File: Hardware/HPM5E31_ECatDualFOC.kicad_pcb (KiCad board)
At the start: 4 copper layers, 85 x 113.4 mm, 453 parts, among them J1 Conn_Coaxial, J13 PHB2.0-02-20PWZ, J14 PHB2.0-02-20PWZ, J15 RJ45_Hanrun_HR911105A_Horizon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, J16 RJ45_Hanrun_HR911105A_Horizon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, J17 WAFER-GH1.25-4PWB, J18 WAFER-GH1.25-4PWB, J19 WAFER-GH1.25-4PWB, J2 Conn_Coaxial, J20 WAFER-GH1.25-2PWB, J21 WAFER-GH1.25-2PWB, J22 USB_B, J23 WAFER-GH1.25-4PWB, J24 WAFER-GH1.25-4PLB, J3 WAFER-ZH1.5-4PWB, J4 Conn_02x05_Odd_Even, J5 WAFER-GH1.25-6PWB, J6 Conn_02x05_Odd_Even, K1 DSHP02TSGET, Q1 CSD19532Q5B, Q10 CSD19532Q5B, Q11 CSD19532Q5B, Q12 CSD19532Q5B, Q13 CSD19532Q5B, Q14 NCE01ND03S, Q15 CSD19532Q5B, Q16 NCE01ND03S, Q2 CSD19532Q5B, Q3 CSD19532Q5B, Q4 CSD19532Q5B, Q5 CSD19532Q5B, Q6 CSD19532Q5B, Q7 CSD19532Q5B, Q8 CSD19532Q5B, Q9 CSD19532Q5B, U1 TXS0108ERGYR, U10 REF3030AIDBZR, U11 MX25L12833FM2I-10G, U12 UCC27282DRCR, U13 INA240A1PWR, U14 UCC27282DRCR, U15 INA240A1PWR, U16 UCC27282DRCR, U17 INA240A1PWR, U18 74LVC1G08, U19 INA240A1PWR, U2 TXB0104RUTR, U20 UCC27282DRCR, U21 INA240A1PWR, U22 UCC27282DRCR, U23 INA240A1PWR, U24 UCC27282DRCR, U25 INA240A1PWR, U26 74LVC1G08, U27 INA240A1PWR, U28 PY32F002BF15U, U29 EG2104, U3 HPM5E31IGN1, U30 ZX-HY2.0-2PWT, U31 RT9193-33GB-MS, U32 EG2104, U33 ZX-HY2.0-2PWT, U34 M3, U35 RS622XTDE8, U36 74LVC1G08, U37 74LVC1G08, U38 M3, U39 MS2575T, U4 LM5164DDAR, U40 MS2575T, U41 TXB0104RUTR, U42 MS2575T, U43 MS2575T, U44 TXB0104RUTR, U45 JL1111-N032I, U46 M3, U47 M3, U48 JL1111-N032I, U49 SP3485EN-L/TR, U5 MP1605GTF-Z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

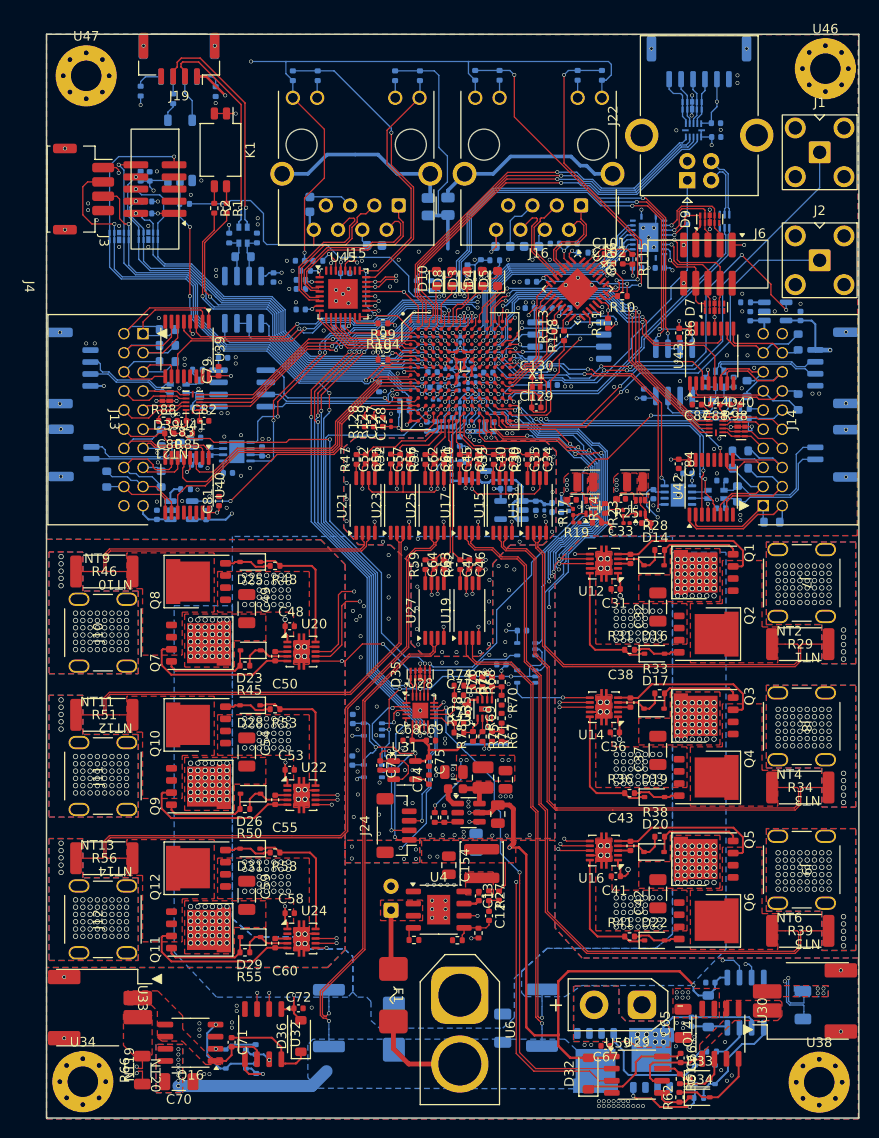
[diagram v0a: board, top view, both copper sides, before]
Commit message: 添加母线电压测量
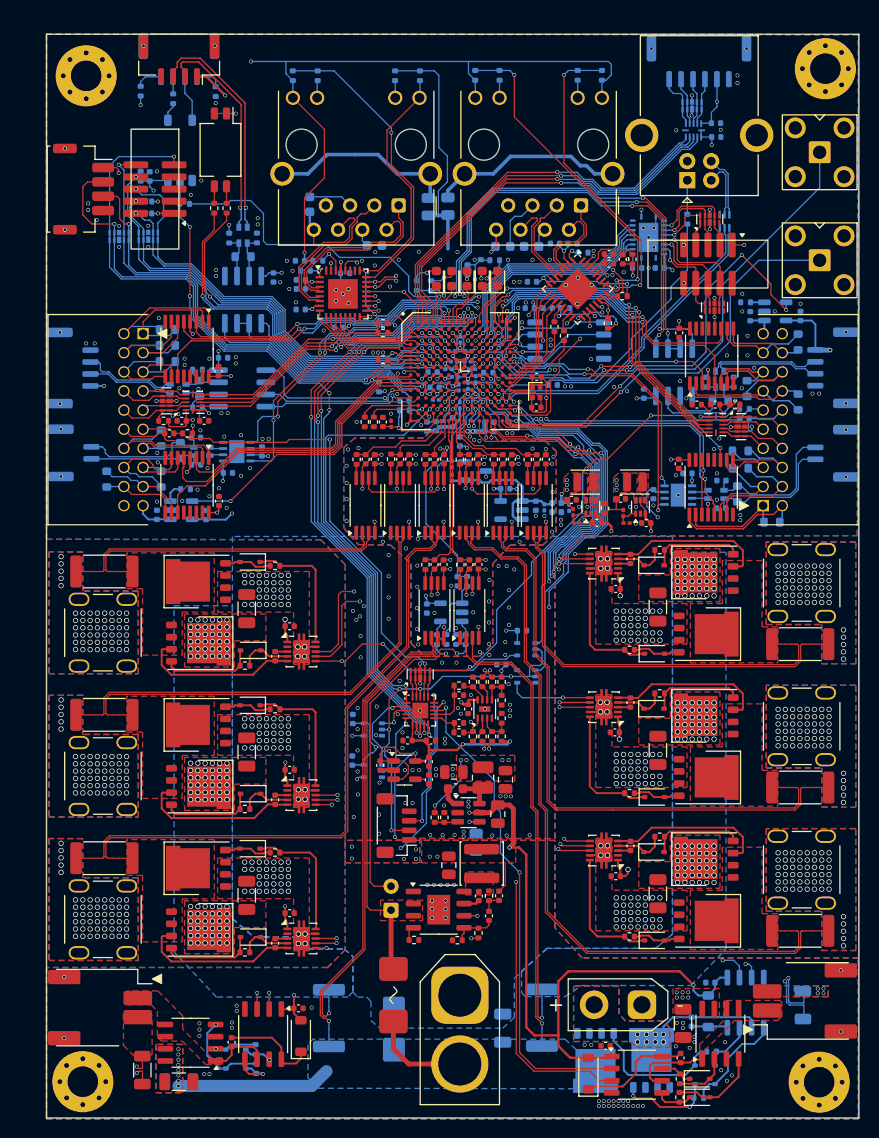
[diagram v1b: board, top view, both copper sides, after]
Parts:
- added C27: 2.2nF,50V, Capacitor_SMD:C_0402_1005Metric, B.Cu at (104.8, 126.6)
- added C28: 100nF,16V, Capacitor_SMD:C_0402_1005Metric, B.Cu at (101.6, 129.4)
- added R32: 33R,1%, Resistor_SMD:R_0402_1005Metric, B.Cu at (105.8, 126.6)
- added R37: 1K,1%, Resistor_SMD:R_0402_1005Metric, B.Cu at (103.7, 132.7)
- added R44: 1K,1%, Resistor_SMD:R_0402_1005Metric, B.Cu at (104.7, 132.7)
- added R49: 50K,1%, Resistor_SMD:R_0402_1005Metric, B.Cu at (105.7, 132.7)
- added R54: 50K,1%, Resistor_SMD:R_0402_1005Metric, B.Cu at (102.7, 132.7)
- added U61: RS621PXF, Package_TO_SOT_SMD:SOT-23-5, B.Cu at (104.2, 129.8)
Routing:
- net /POWER_SUPPLY/VBUS_F: track 6.25 -> 43.9 mm, vias 0 -> 1
- net GNDPWR: track 121.1 -> 153.9 mm, vias 265 -> 266
- net PF27: track 0.57 -> 21.6 mm, vias 1 -> 2
- net VDDA: track 58.2 -> 69.7 mm, vias 10 -> 11
- net Net-(U61-OUT): track 0.00 -> 6.56 mm
- net Net-(U61-+IN): track 0.00 -> 2.97 mm
- net Net-(U61--IN): track 0.00 -> 2.97 mm
- net /MB_TEMP: track 55.4 -> 54.7 mm
- net GNDA: track 57.6 -> 57.9 mm, vias 55 -> 57
